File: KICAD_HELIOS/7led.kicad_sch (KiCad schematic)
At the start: 7 parts

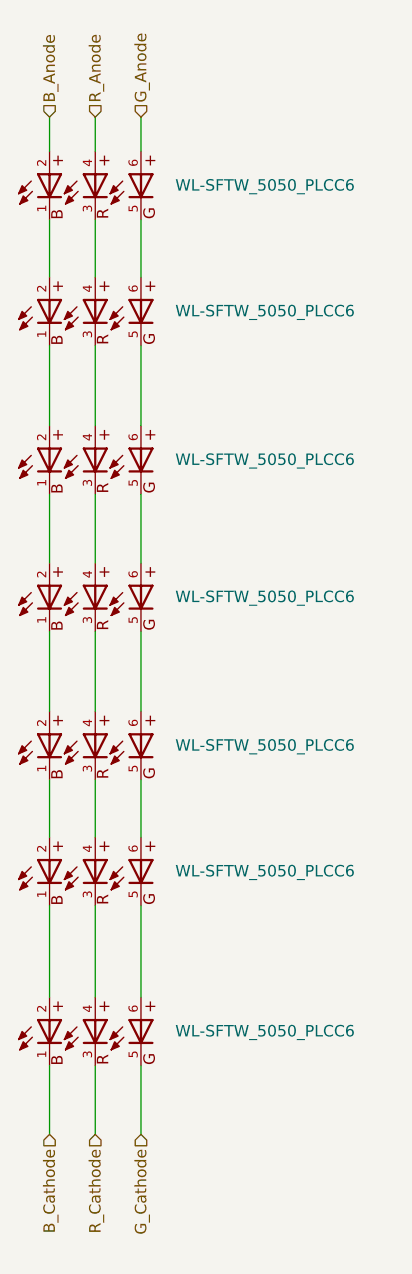
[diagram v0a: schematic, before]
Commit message: Fix: correction erreurs schéma, maj empreintes et ajout notes
- Résolution de toutes les erreurs ERC du schéma.
- Mise à jour des empreintes (Importation d'empreintes non présentes dans KiCad, composants passifs...).
- Ajout de Warning_KiCad_fichier_temporaire.md : liste des questions et problèmes à régler.
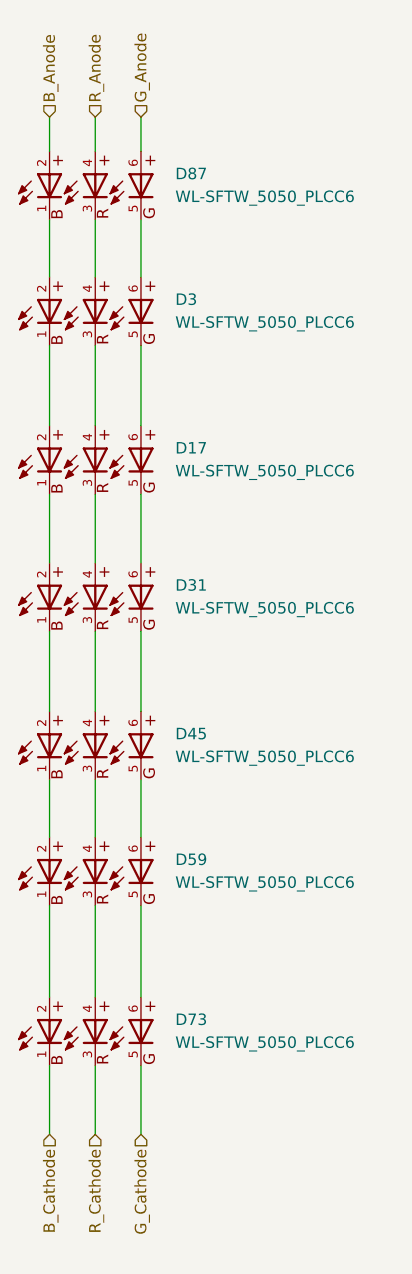
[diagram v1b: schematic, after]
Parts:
- removed D4, D5, D6, D7, D8, D9: WL-SFTW_5050_PLCC6, WL-SFTW_5050_PLCC6:WL-SFTW_5050_PLCC6, symbol WL-SFTW_5050_PLCC6:WL-SFTW_5050_PLCC6
- added D17, D31, D45, D59, D73, D87: WL-SFTW_5050_PLCC6, LED:WL-SFTW_5050_PLCC6, symbol WL-SFTW_5050_PLCC6:WL-SFTW_5050_PLCC6
- D3: footprint WL-SFTW_5050_PLCC6:WL-SFTW_5050_PLCC6 -> LED:WL-SFTW_5050_PLCC6; Availability In Stock -> (none); DigiKey_Part_Number (none) -> 732-12000-1-ND; Price None -> (none)
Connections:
- net B_Anode: now also D87.2; no longer D3.2
- net B_Cathode: now also D73.1
- net G_Anode: now also D87.6; no longer D3.6
- net G_Cathode: now also D73.5
- net R_Anode: now also D87.4; no longer D3.4
- net R_Cathode: now also D73.3
- net at D3.1: now also D17.2
- net at D3.3: now also D17.4
- net at D3.5: now also D17.6
- new net: D59.1, D73.2
- new net: D45.1, D59.2
- new net: D59.3, D73.4
- new net: D45.3, D59.4
- new net: D59.5, D73.6
- new net: D45.5, D59.6
- new net: D3.2, D87.1
- new net: D3.4, D87.3
- new net: D3.6, D87.5
- new net: D31.1, D45.2
- new net: D17.1, D31.2
- new net: D31.3, D45.4
- new net: D17.3, D31.4
- new net: D31.5, D45.6
- new net: D17.5, D31.6

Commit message: update pcb
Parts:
- renumbered D87 to D401, D3 to D402, D17 to D403, D31 to D404, D45 to D405, D59 to D406, D73 to D407
